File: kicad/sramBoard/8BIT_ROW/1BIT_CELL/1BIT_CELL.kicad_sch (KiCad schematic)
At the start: 8 parts, among them Q1 NMOS, Q2 NMOS, Q3 PMOS, Q4 NMOS, Q5 PMOS, Q6 NMOS, Q7 NMOS, Q8 NMOS

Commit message: cdcdcdcdcdcdcdcdcdcdc
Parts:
- Q1, Q2, Q4, Q6, Q7, Q8: footprint Package_TO_SOT_SMD:SOT-23 -> easyeda2kicad:SOT-23-N
- Q3, Q5: footprint Package_TO_SOT_SMD:SOT-23 -> easyeda2kicad:SOT-23-P
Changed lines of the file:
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@@
 			)
 		)
-		(property "Footprint" "Package_TO_SOT_SMD:SOT-23"
+		(property "Footprint" "easyeda2kicad:SOT-23-P"
 			(at 123.19 82.55 0)
 			(hide yes)
@@
 			)
 		)
-		(property "Footprint" "Package_TO_SOT_SMD:SOT-23"
+		(property "Footprint" "easyeda2kicad:SOT-23-N"
 			(at 77.47 92.71 0)
 			(hide yes)
@@
 			)
 		)
-		(property "Footprint" "Package_TO_SOT_SMD:SOT-23"
+		(property "Footprint" "easyeda2kicad:SOT-23-N"
 			(at 107.95 95.25 0)
 			(hide yes)
@@
 			)
 		)
-		(property "Footprint" "Package_TO_SOT_SMD:SOT-23"
+		(property "Footprint" "easyeda2kicad:SOT-23-N"
 			(at 123.19 95.25 0)
 			(hide yes)
@@
 			)
 		)
-		(property "Footprint" "Package_TO_SOT_SMD:SOT-23"
+		(property "Footprint" "easyeda2kicad:SOT-23-N"
 			(at 152.4 90.17 0)
 			(hide yes)
@@
 			)
 		)
-		(property "Footprint" "Package_TO_SOT_SMD:SOT-23"
+		(property "Footprint" "easyeda2kicad:SOT-23-N"
 			(at 72.39 92.71 0)
 			(hide yes)
@@
 			)
 		)
-		(property "Footprint" "Package_TO_SOT_SMD:SOT-23"
+		(property "Footprint" "easyeda2kicad:SOT-23-P"
 			(at 107.95 82.55 0)
 			(hide yes)
@@
 			)
 		)
-		(property "Footprint" "Package_TO_SOT_SMD:SOT-23"
+		(property "Footprint" "easyeda2kicad:SOT-23-N"
 			(at 157.48 90.17 0)
 			(hide yes)

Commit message: add pmos resistors
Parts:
- added R1: 47R, Resistor_SMD:R_0603_1608Metric, symbol Device:R
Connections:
- net +5V: now also R1.1; no longer Q3.3 (S), Q5.3 (S)
- new net: Q3.3 (S), Q5.3 (S), R1.2

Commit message: finish main pcb
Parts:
- added D1: LED, LED_SMD:LED_0805_2012Metric_Pad1.15x1.40mm_HandSolder, symbol Device:LED
- added Q5: NMOS, easyeda2kicad:SOT-23-N, symbol Simulation_SPICE:NMOS
- added R1: 220R, Resistor_SMD:R_0603_1608Metric_Pad0.98x0.95mm_HandSolder, symbol Device:R
- Q1, Q2, Q4: LCSC Part # (none) -> C49308282
- Q3: LCSC Part # (none) -> C41384537
- Q6: renamed from Q5; LCSC Part # (none) -> C41384537
- Q7: renamed from Q6; LCSC Part # (none) -> C49308282
- Q8: renamed from Q7; LCSC Part # (none) -> C49308282
- Q9: renamed from Q8; LCSC Part # (none) -> C49308282
- R2: renamed from R1; LCSC Part # (none) -> C54531463
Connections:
- net +5V: now also Q5.1 (D)
- net GND: now also D1.1 (K)
- net at Q2.3 (S), Q3.2 (G), Q4.2 (G)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: now also Q5.2 (G)
- new net: Q5.3 (S), R1.1
- new net: D1.2 (A), R1.2

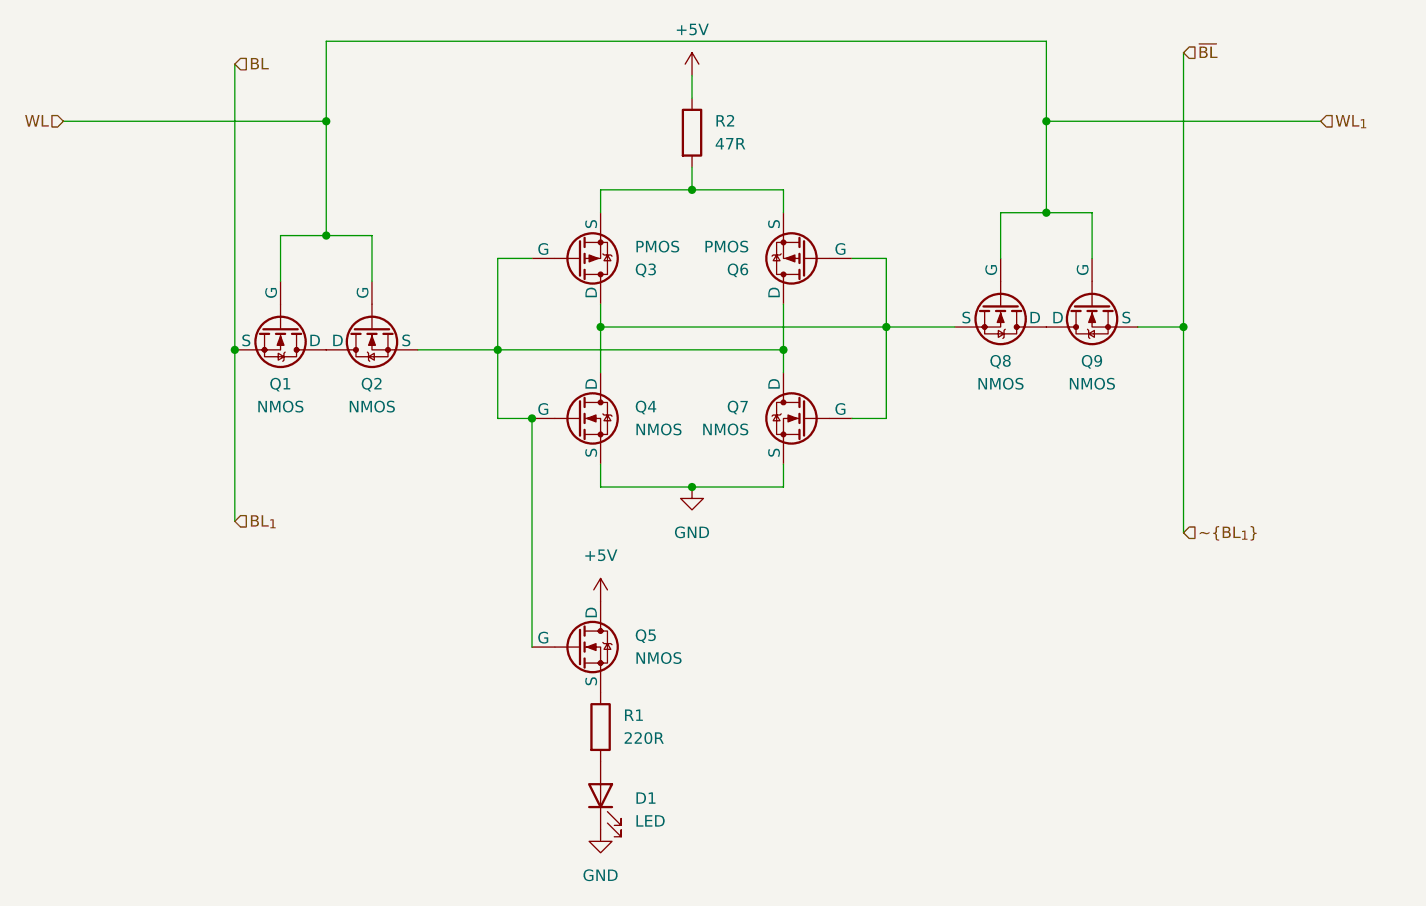
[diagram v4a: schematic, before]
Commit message: fix main ram board
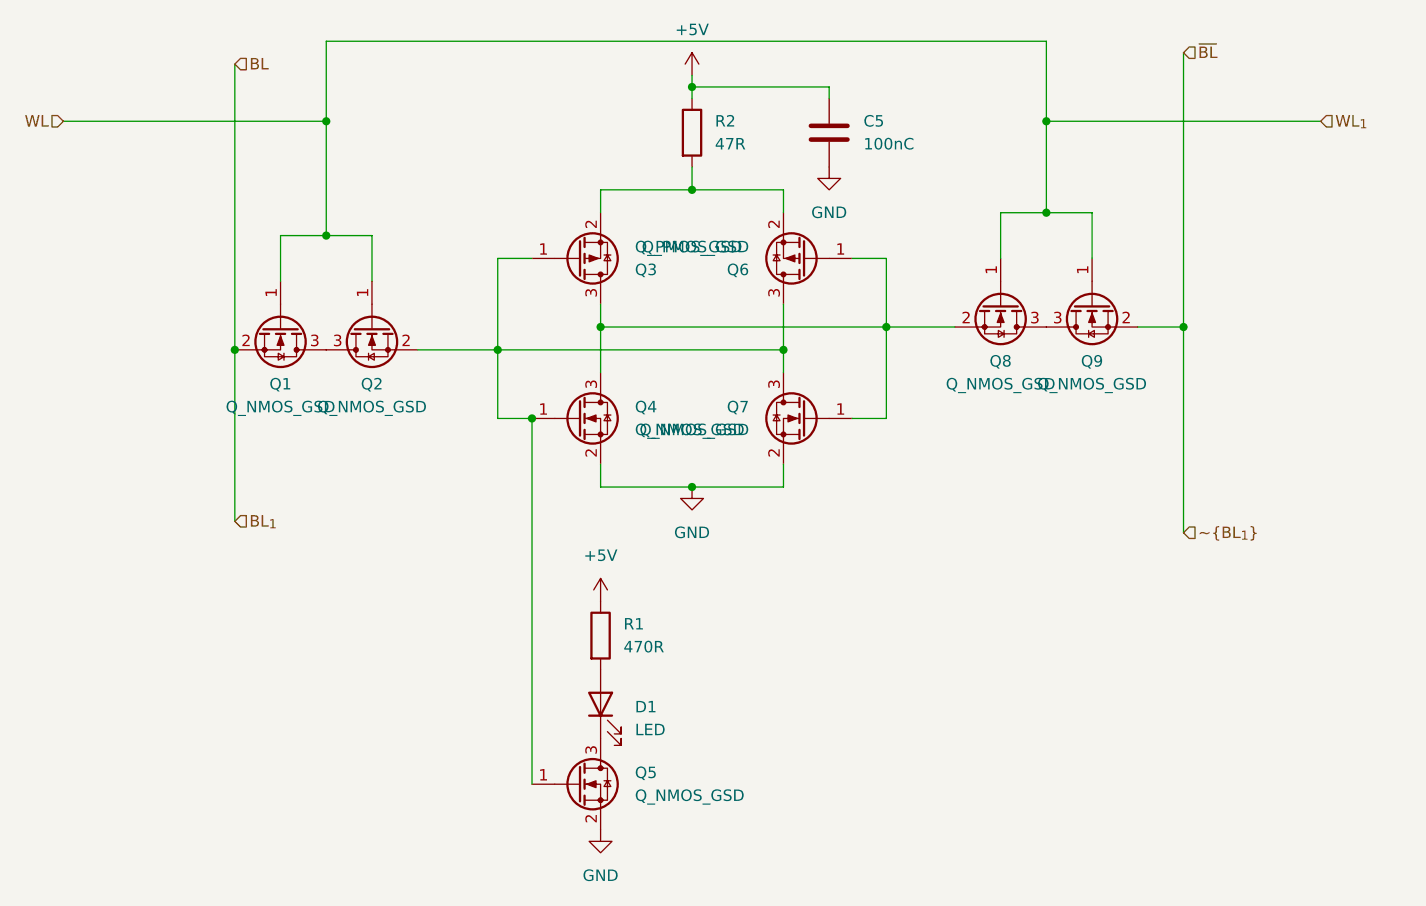
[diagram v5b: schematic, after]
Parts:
- removed Q5: NMOS, easyeda2kicad:SOT-23-N, symbol Simulation_SPICE:NMOS
- added C5: 100nC, Capacitor_SMD:C_0603_1608Metric, symbol Device:C
- added Q5: Q_NMOS_GSD, easyeda2kicad:SOT-23-N, symbol Transistor_FET:Q_NMOS_GSD
- Q1, Q2, Q4, Q7, Q8, Q9: value NMOS -> Q_NMOS_GSD; symbol Simulation_SPICE:NMOS -> Transistor_FET:Q_NMOS_GSD
- Q3, Q6: value PMOS -> Q_PMOS_GSD; symbol Simulation_SPICE:PMOS -> Transistor_FET:Q_PMOS_GSD
- R1: value 220R -> 470R; footprint Resistor_SMD:R_0603_1608Metric_Pad0.98x0.95mm_HandSolder -> Resistor_SMD:R_0805_2012Metric_Pad1.20x1.40mm_HandSolder
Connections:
- net +5V: now also R1.1, C5.1
- net BL: now also Q1.2 (S); no longer Q1.3 (S)
- net GND: now also Q4.2 (S), Q7.2 (S), C5.2, Q5.2 (S); no longer D1.1 (K), Q4.3 (S), Q7.3 (S)
- net WL: now also Q1.1 (G), Q2.1 (G), Q8.1 (G), Q9.1 (G); no longer Q1.2 (G), Q2.2 (G), Q8.2 (G), Q9.2 (G)
- net ~{BL_{1}}: now also Q9.2 (S); no longer Q9.3 (S)
- new net: Q3.3 (D), Q4.3 (D), Q6.1 (G), Q7.1 (G), Q8.2 (S)
- new net: Q3.2 (S), Q6.2 (S), R2.2
- new net: Q2.2 (S), Q3.1 (G), Q4.1 (G), Q5.1 (G), Q6.3 (D), Q7.3 (D)
- new net: Q1.3 (D), Q2.3 (D)
- new net: D1.1 (K), Q5.3 (D)
- new net: Q8.3 (D), Q9.3 (D)

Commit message: Add breakout board through holes on main ram board
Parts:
- added J2: Conn_01x02_Pin, Connector_PinHeader_1.00mm:PinHeader_1x02_P1.00mm_Vertical, symbol Connector:Conn_01x02_Pin
- C5: footprint Capacitor_SMD:C_0603_1608Metric -> Capacitor_SMD:C_0805_2012Metric
- D1: footprint LED_SMD:LED_0805_2012Metric_Pad1.15x1.40mm_HandSolder -> Capacitor_SMD:C_0805_2012Metric
- R7: renamed from R1; value 470R -> 360R
- renumbered R2 to R8
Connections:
- net at Q3.3 (D), Q4.3 (D), Q6.1 (G)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: now also J2.2 (Pin_2)
- net at Q2.2 (S), Q3.1 (G), Q4.1 (G)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: now also J2.1 (Pin_1)

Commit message: finish main input board
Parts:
- R2: renamed from R7; value 360R -> 180R
- renumbered C5 to C1, J2 to J1, Q6 to Q5, Q7 to Q6, Q8 to Q7, Q9 to Q8, Q5 to Q9, R8 to R1
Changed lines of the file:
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@@
 		(in_pos_files yes)
 		(dnp no)
-		(property "Reference" "Q6"
+		(property "Reference" "Q5"
 			(at 121.92 81.2801 0)
 			(show_name no)
@@
 		(dnp no)
 		(fields_autoplaced yes)
-		(property "Reference" "R8"
+		(property "Reference" "R1"
 			(at 118.11 64.7699 0)
 			(show_name no)
@@
 		(dnp no)
 		(fields_autoplaced yes)
-		(property "Reference" "J2"
+		(property "Reference" "J1"
 			(at 127 120.0149 90)
 			(show_name no)
@@
 		(dnp no)
 		(fields_autoplaced yes)
-		(property "Reference" "C5"
+		(property "Reference" "C1"
 			(at 134.62 64.7699 0)
 			(show_name no)
@@
 		(dnp no)
 		(fields_autoplaced yes)
-		(property "Reference" "Q7"
+		(property "Reference" "Q6"
 			(at 121.92 96.5199 0)
 			(show_name no)
@@
 		(dnp no)
 		(fields_autoplaced yes)
-		(property "Reference" "#PWR016"
+		(property "Reference" "#PWR01"
 			(at 115.57 63.5 0)
 			(hide yes)
@@
 		(dnp no)
 		(fields_autoplaced yes)
-		(property "Reference" "Q5"
+		(property "Reference" "Q9"
 			(at 109.22 137.1599 0)
 			(show_name no)
@@
 		(dnp no)
 		(fields_autoplaced yes)
-		(property "Reference" "#PWR018"
+		(property "Reference" "#PWR05"
 			(at 130.81 76.2 0)
 			(hide yes)
@@
 		(dnp no)
 		(fields_autoplaced yes)
-		(property "Reference" "Q8"
+		(property "Reference" "Q7"
 			(at 149.86 91.44 90)
 			(show_name no)
@@
 		(dnp no)
 		(fields_autoplaced yes)
-		(property "Reference" "R7"
+		(property "Reference" "R2"
 			(at 107.95 120.6499 0)
 			(show_name no)
@@
 			)
 		)
-		(property "Value" "360R"
+		(property "Value" "180R"
 			(at 107.95 123.1899 0)
 			(show_name no)
@@
 		(dnp no)
 		(fields_autoplaced yes)
-		(property "Reference" "#PWR014"
+		(property "Reference" "#PWR03"
 			(at 105.41 121.92 0)
 			(hide yes)
@@
 		(dnp no)
 		(fields_autoplaced yes)
-		(property "Reference" "#PWR017"
+		(property "Reference" "#PWR02"
 			(at 115.57 111.76 0)
 			(hide yes)
@@
 		(dnp no)
 		(fields_autoplaced yes)
-		(property "Reference" "#PWR015"
+		(property "Reference" "#PWR04"
 			(at 105.41 149.86 0)
 			(hide yes)
@@
 		(in_pos_files yes)
 		(dnp no)
-		(property "Reference" "Q9"
+		(property "Reference" "Q8"
 			(at 160.02 91.44 90)
 			(show_name no)
@@
 		)
 	)
+	(embedded_fonts no)
 )

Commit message: update bom, add more capacitors
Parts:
- renumbered C1 to C5, J1 to J2, Q9 to Q5, Q5 to Q6, Q6 to Q7, Q7 to Q8, Q8 to Q9, R2 to R7, R1 to R8
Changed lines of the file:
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@@
 		(in_pos_files yes)
 		(dnp no)
-		(property "Reference" "Q5"
+		(property "Reference" "Q6"
 			(at 121.92 81.2801 0)
 			(show_name no)
@@
 		(dnp no)
 		(fields_autoplaced yes)
-		(property "Reference" "R1"
+		(property "Reference" "R8"
 			(at 118.11 64.7699 0)
 			(show_name no)
@@
 		(dnp no)
 		(fields_autoplaced yes)
-		(property "Reference" "J1"
+		(property "Reference" "J2"
 			(at 127 120.0149 90)
 			(show_name no)
@@
 		(dnp no)
 		(fields_autoplaced yes)
-		(property "Reference" "C1"
+		(property "Reference" "C5"
 			(at 134.62 64.7699 0)
 			(show_name no)
@@
 		(dnp no)
 		(fields_autoplaced yes)
-		(property "Reference" "Q6"
+		(property "Reference" "Q7"
 			(at 121.92 96.5199 0)
 			(show_name no)
@@
 		(dnp no)
 		(fields_autoplaced yes)
-		(property "Reference" "#PWR01"
+		(property "Reference" "#PWR016"
 			(at 115.57 63.5 0)
 			(hide yes)
@@
 		(dnp no)
 		(fields_autoplaced yes)
-		(property "Reference" "Q9"
+		(property "Reference" "Q5"
 			(at 109.22 137.1599 0)
 			(show_name no)
@@
 		(dnp no)
 		(fields_autoplaced yes)
-		(property "Reference" "#PWR05"
+		(property "Reference" "#PWR018"
 			(at 130.81 76.2 0)
 			(hide yes)
@@
 		(dnp no)
 		(fields_autoplaced yes)
-		(property "Reference" "Q7"
+		(property "Reference" "Q8"
 			(at 149.86 91.44 90)
 			(show_name no)
@@
 		(dnp no)
 		(fields_autoplaced yes)
-		(property "Reference" "R2"
+		(property "Reference" "R7"
 			(at 107.95 120.6499 0)
 			(show_name no)
@@
 		(dnp no)
 		(fields_autoplaced yes)
-		(property "Reference" "#PWR03"
+		(property "Reference" "#PWR014"
 			(at 105.41 121.92 0)
 			(hide yes)
@@
 		(dnp no)
 		(fields_autoplaced yes)
-		(property "Reference" "#PWR02"
+		(property "Reference" "#PWR017"
 			(at 115.57 111.76 0)
 			(hide yes)
@@
 		(dnp no)
 		(fields_autoplaced yes)
-		(property "Reference" "#PWR04"
+		(property "Reference" "#PWR015"
 			(at 105.41 149.86 0)
 			(hide yes)
@@
 		(in_pos_files yes)
 		(dnp no)
-		(property "Reference" "Q8"
+		(property "Reference" "Q9"
 			(at 160.02 91.44 90)
 			(show_name no)
@@
 		)
 	)
-	(embedded_fonts no)
 )
